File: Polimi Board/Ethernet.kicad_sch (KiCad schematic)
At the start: 20 parts, among them J6 RJ45_Wuerth_7499010121A, U3 LAN8742A, Y2 25MHz

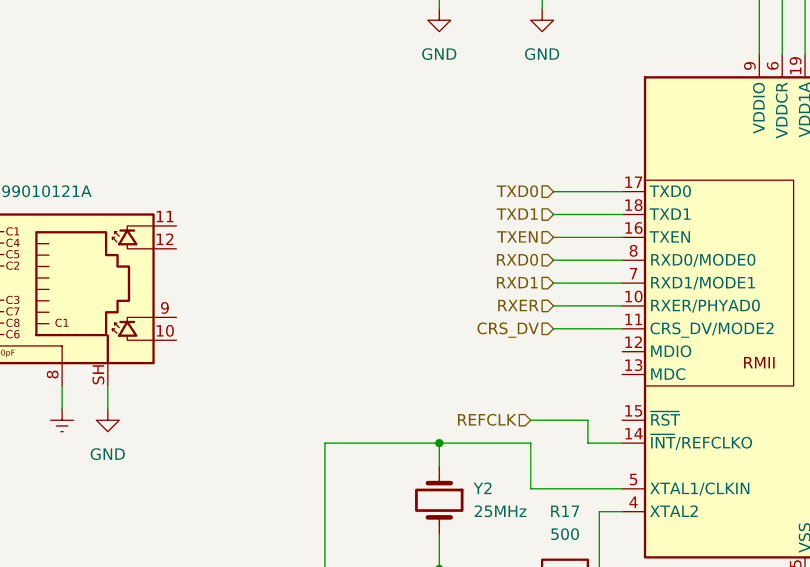
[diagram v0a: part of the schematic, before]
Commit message: Added GPIOs
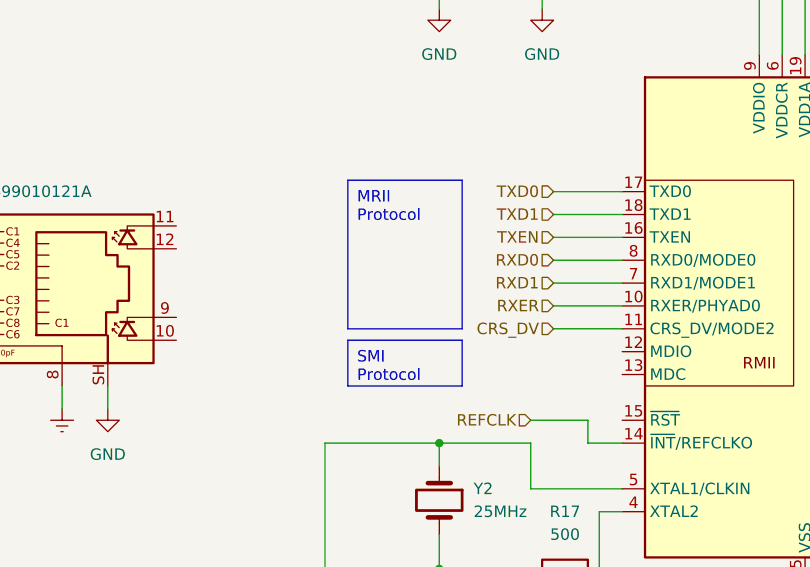
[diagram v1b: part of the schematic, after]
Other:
- company: (none) -> Politecnico di Milano
- title: (none) -> Polimi Board 
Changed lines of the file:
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@@
 (kicad_sch (version 20230121) (generator eeschema)
   (paper "A4")
+  (title_block
+    (title "Polimi Board ")
+    (date "2024-04-09")
+    (rev "1.0")
+    (company "Politecnico di Milano")
+    (comment 1 "Embedded Systems")
+    (comment 2 "ing. Zaccaria Eliseo Carrettoni")
+  )
   (junction (at 199.39 72.39) (diameter 0) (color 0 0 0 0)
   )
@@
     (stroke (width 0) (type default))
   )
+  (text_box "MRII\nProtocol\n"
+    (at 101.6 88.9 0) (size 12.7 16.51)
+    (stroke (width 0) (type default))
+    (fill (type none))
+    (effects (font (size 1.27 1.27)) (justify left top))
+  )
+  (text_box "SMI \nProtocol\n"
+    (at 101.6 106.68 0) (size 12.7 5.08)
+    (stroke (width 0) (type default))
+    (fill (type none))
+    (effects (font (size 1.27 1.27)) (justify left top))
+  )
   (label "TXN" (at 34.29 99.06 180) (fields_autoplaced)

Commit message: Finish schematic part
To be reviewd
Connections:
- no-connect marks 0 -> 8

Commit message: Fatte modifiche
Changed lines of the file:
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@@
   (title_block
     (title "Polimi Board ")
-    (date "2024-04-24")
-    (rev "1.0")
+    (date "2024-04-29")
+    (rev "2.0")
     (company "Politecnico di Milano")
     (comment 1 "Embedded Systems Project")
@@
     (stroke (width 0) (type default))
   )
-  (text_box "MRII\nProtocol\n"
+  (text_box "RMII\nProtocol\n"
     (at 101.6 88.9 0) (size 12.7 16.51)
     (stroke (width 0) (type default))

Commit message: Update the design with new specifications
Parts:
- removed C22, C23: 10pF, symbol Device:C
- removed R17: 500, symbol Device:R
- removed Y2: 25MHz, symbol Device:Crystal
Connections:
- net MCO: now reaches U3.5 (XTAL1/CLKIN)
- no-connect marks 8 -> 9
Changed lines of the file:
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@@
   (title_block
     (title "Polimi Board ")
-    (date "2024-04-29")
+    (date "2024-05-14")
     (rev "2.0")
     (company "Politecnico di Milano")
@@
   (junction (at 123.19 34.29) (diameter 0) (color 0 0 0 0)
   )
-  (junction (at 111.76 118.11) (diameter 0) (color 0 0 0 0)
-  )
   (junction (at 204.47 97.79) (diameter 0) (color 0 0 0 0)
   )
   (junction (at 165.1 59.69) (diameter 0) (color 0 0 0 0)
   )
-  (junction (at 111.76 140.97) (diameter 0) (color 0 0 0 0)
-  )
   (junction (at 26.67 96.52) (diameter 0) (color 0 0 0 0)
   )
@@
   )
   (junction (at 204.47 72.39) (diameter 0) (color 0 0 0 0)
-  )
-  (junction (at 111.76 132.08) (diameter 0) (color 0 0 0 0)
   )
   (junction (at 123.19 59.69) (diameter 0) (color 0 0 0 0)
@@
   (no_connect (at 132.08 107.95))
   (no_connect (at 132.08 115.57))
+  (no_connect (at 132.08 125.73))
   (no_connect (at 82.55 106.68))
   (no_connect (at 82.55 104.14))
@@
     (stroke (width 0) (type default))
   )
-  (wire (pts (xy 111.76 128.27) (xy 111.76 132.08))
-    (stroke (width 0) (type default))
-  )
-  (wire (pts (xy 121.92 123.19) (xy 121.92 118.11))
-    (stroke (width 0) (type default))
-  )
   (wire (pts (xy 165.1 67.31) (xy 165.1 69.85))
     (stroke (width 0) (type default))
@@
     (stroke (width 0) (type default))
   )
-  (wire (pts (xy 111.76 139.7) (xy 111.76 140.97))
-    (stroke (width 0) (type default))
-  )
   (wire (pts (xy 204.47 97.79) (xy 207.01 97.79))
     (stroke (width 0) (type default))
@@
     (stroke (width 0) (type default))
   )
-  (wire (pts (xy 128.27 118.11) (xy 132.08 118.11))
+  (wire (pts (xy 124.46 118.11) (xy 132.08 118.11))
     (stroke (width 0) (type default))
   )
@@
     (stroke (width 0) (type default))
   )
-  (wire (pts (xy 121.92 115.57) (xy 128.27 115.57))
-    (stroke (width 0) (type default))
-  )
-  (wire (pts (xy 132.08 125.73) (xy 129.54 125.73))
-    (stroke (width 0) (type default))
-  )
   (wire (pts (xy 34.29 101.6) (xy 39.37 101.6))
     (stroke (width 0) (type default))
   )
-  (wire (pts (xy 99.06 139.7) (xy 99.06 140.97))
+  (wire (pts (xy 124.46 123.19) (xy 132.08 123.19))
     (stroke (width 0) (type default))
   )
@@
     (stroke (width 0) (type default))
   )
-  (wire (pts (xy 111.76 118.11) (xy 111.76 120.65))
-    (stroke (width 0) (type default))
-  )
   (wire (pts (xy 74.93 111.76) (xy 74.93 124.46))
     (stroke (width 0) (type default))
@@
     (stroke (width 0) (type default))
   )
-  (wire (pts (xy 129.54 125.73) (xy 129.54 132.08))
-    (stroke (width 0) (type default))
-  )
   (wire (pts (xy 26.67 104.14) (xy 39.37 104.14))
     (stroke (width 0) (type default))
@@
     (stroke (width 0) (type default))
   )
-  (wire (pts (xy 128.27 115.57) (xy 128.27 118.11))
-    (stroke (width 0) (type default))
-  )
   (wire (pts (xy 123.19 67.31) (xy 123.19 69.85))
     (stroke (width 0) (type default))
@@
     (stroke (width 0) (type default))
   )
-  (wire (pts (xy 111.76 132.08) (xy 121.92 132.08))
-    (stroke (width 0) (type default))
-  )
   (wire (pts (xy 170.18 100.33) (xy 213.36 100.33))
     (stroke (width 0) (type default))
@@
     (stroke (width 0) (type default))
   )
-  (wire (pts (xy 111.76 118.11) (xy 99.06 118.11))
-    (stroke (width 0) (type default))
-  )
   (wire (pts (xy 124.46 90.17) (xy 132.08 90.17))
     (stroke (width 0) (type default))
   )
-  (wire (pts (xy 99.06 118.11) (xy 99.06 132.08))
-    (stroke (width 0) (type default))
-  )
-  (wire (pts (xy 132.08 123.19) (xy 121.92 123.19))
-    (stroke (width 0) (type default))
-  )
   (wire (pts (xy 194.31 82.55) (xy 194.31 95.25))
     (stroke (width 0) (type default))
   )
-  (wire (pts (xy 99.06 140.97) (xy 111.76 140.97))
-    (stroke (width 0) (type default))
-  )
   (wire (pts (xy 175.26 123.19) (xy 175.26 127))
     (stroke (width 0) (type default))
@@
   )
   (wire (pts (xy 170.18 95.25) (xy 194.31 95.25))
-    (stroke (width 0) (type default))
-  )
-  (wire (pts (xy 121.92 118.11) (xy 111.76 118.11))
-    (stroke (width 0) (type default))
-  )
-  (wire (pts (xy 111.76 140.97) (xy 111.76 142.24))
     (stroke (width 0) (type default))
   )
@@
     (effects (font (size 1.27 1.27)) (justify left top))
   )
+  (text_box "MCO\nClock from MCU\n"
+    (at 101.6 119.38 0) (size 12.7 7.62)
+    (stroke (width 0) (type default))
+    (fill (type none))
+    (effects (font (size 1.27 1.27)) (justify left top))
+  )
   (label "TXN" (at 34.29 99.06 180) (fields_autoplaced)
     (effects (font (size 1.27 1.27)) (justify right bottom))
@@
     (effects (font (size 1.27 1.27)) (justify right bottom))
   )
-  (hierarchical_label "REFCLK" (shape input) (at 121.92 115.57 180) (fields_autoplaced)
+  (hierarchical_label "REFCLK" (shape input) (at 124.46 118.11 180) (fields_autoplaced)
     (effects (font (size 1.27 1.27)) (justify right))
   )
@@
     (effects (font (size 1.27 1.27)) (justify right))
   )
+  (hierarchical_label "MCO" (shape input) (at 124.46 123.19 180) (fields_autoplaced)
+    (effects (font (size 1.27 1.27)) (justify right))
+  )
   (hierarchical_label "RXER" (shape input) (at 124.46 102.87 180) (fields_autoplaced)
     (effects (font (size 1.27 1.27)) (justify right))
@@
     )
   )
-  (symbol (lib_id "Device:R") (at 125.73 132.08 90) (unit 1)
-    (in_bom yes) (on_board yes) (dnp no) (fields_autoplaced)
-    (property "Reference" "R17" (at 125.73 125.73 90)
-      (effects (font (size 1.27 1.27)))
-    )
-    (property "Value" "500" (at 125.73 128.27 90)
-      (effects (font (size 1.27 1.27)))
-    )
-    (property "Footprint" "" (at 125.73 133.858 90)
-      (effects (font (size 1.27 1.27)) hide)
-    )
-    (property "Datasheet" "~" (at 125.73 132.08 0)
-      (effects (font (size 1.27 1.27)) hide)
-    )
-    (pin "2")
-    (pin "1")
-    (instances
-      (project "Polimi Board"
-        (path "/319fe76e-1f98-44b3-99b0-af1a9ad7322c/2985c2dc-97fe-4379-8500-18b000a93b2c"
-          (reference "R17") (unit 1)
-        )
-      )
-    )
-  )
   (symbol (lib_id "Device:R") (at 204.47 78.74 0) (unit 1)
     (in_bom yes) (on_board yes) (dnp no) (fields_autoplaced)
@@
         (path "/319fe76e-1f98-44b3-99b0-af1a9ad7322c/2985c2dc-97fe-4379-8500-18b000a93b2c"
           (reference "#PWR046") (unit 1)
-        )
-      )
-    )
-  )
-  (symbol (lib_id "power:GND") (at 111.76 142.24 0) (unit 1)
-    (in_bom yes) (on_board yes) (dnp no) (fields_autoplaced)
-    (property "Reference" "#PWR052" (at 111.76 148.59 0)
-      (effects (font (size 1.27 1.27)) hide)
-    )
-    (property "Value" "GND" (at 111.76 147.32 0)
-      (effects (font (size 1.27 1.27)))
-    )
-    (property "Footprint" "" (at 111.76 142.24 0)
-      (effects (font (size 1.27 1.27)) hide)
-    )
-    (property "Datasheet" "" (at 111.76 142.24 0)
-      (effects (font (size 1.27 1.27)) hide)
-    )
-    (pin "1")
-    (instances
-      (project "Polimi Board"
-        (path "/319fe76e-1f98-44b3-99b0-af1a9ad7322c/2985c2dc-97fe-4379-8500-18b000a93b2c"
-          (reference "#PWR052") (unit 1)
         )
       )
@@
     )
   )
-  (symbol (lib_id "Device:C") (at 99.06 135.89 0) (unit 1)
-    (in_bom yes) (on_board yes) (dnp no) (fields_autoplaced)
-    (property "Reference" "C23" (at 102.87 134.62 0)
-      (effects (font (size 1.27 1.27)) (justify left))
-    )
-    (property "Value" "10pF" (at 102.87 137.16 0)
-      (effects (font (size 1.27 1.27)) (justify left))
-    )
-    (property "Footprint" "" (at 100.0252 139.7 0)
-      (effects (font (size 1.27 1.27)) hide)
-    )
-    (property "Datasheet" "~" (at 99.06 135.89 0)
-      (effects (font (size 1.27 1.27)) hide)
-    )
-    (pin "1")
-    (pin "2")
-    (instances
-      (project "Polimi Board"
-        (path "/319fe76e-1f98-44b3-99b0-af1a9ad7322c/2985c2dc-97fe-4379-8500-18b000a93b2c"
-          (reference "C23") (unit 1)
-        )
-      )
-    )
-  )
   (symbol (lib_id "power:GND") (at 165.1 69.85 0) (unit 1)
     (in_bom yes) (on_board yes) (dnp no) (fields_autoplaced)
@@
     )
   )
-  (symbol (lib_id "Device:C") (at 111.76 135.89 0) (unit 1)
-    (in_bom yes) (on_board yes) (dnp no) (fields_autoplaced)
-    (property "Reference" "C22" (at 115.57 134.62 0)
-      (effects (font (size 1.27 1.27)) (justify left))
-    )
-    (property "Value" "10pF" (at 115.57 137.16 0)
-      (effects (font (size 1.27 1.27)) (justify left))
-    )
-    (property "Footprint" "" (at 112.7252 139.7 0)
-      (effects (font (size 1.27 1.27)) hide)
-    )
-    (property "Datasheet" "~" (at 111.76 135.89 0)
-      (effects (font (size 1.27 1.27)) hide)
-    )
-    (pin "1")
-    (pin "2")
-    (instances
-      (project "Polimi Board"
-        (path "/319fe76e-1f98-44b3-99b0-af1a9ad7322c/2985c2dc-97fe-4379-8500-18b000a93b2c"
-          (reference "C22") (unit 1)
-        )
-      )
-    )
-  )
   (symbol (lib_id "Device:C") (at 111.76 38.1 0) (unit 1)
     (in_bom yes) (on_board yes) (dnp no) (fields_autoplaced)
@@
         )
       )
-    )
-  )
-  (symbol (lib_id "Device:Crystal") (at 111.76 124.46 270) (unit 1)
-    (in_bom yes) (on_board yes) (dnp no) (fields_autoplaced)
-    (property "Reference" "Y2" (at 115.57 123.19 90)
-      (effects (font (size 1.27 1.27)) (justify left))
-    )
-    (property "Value" "25MHz" (at 115.57 125.73 90)
-      (effects (font (size 1.27 1.27)) (justify left))
-    )
-    (property "Footprint" "" (at 111.76 124.46 0)
-      (effects (font (size 1.27 1.27)) hide)
-    )
-    (property "Datasheet" "~" (at 111.76 124.46 0)
-      (effects (font (size 1.27 1.27)) hide)
-    )
-    (pin "2")
-    (pin "1")
-    (instances
-      (project "Polimi Board"
-        (path "/319fe76e-1f98-44b3-99b0-af1a9ad7322c/2985c2dc-97fe-4379-8500-18b000a93b2c"
-          (reference "Y2") (unit 1)
-        )
-      )

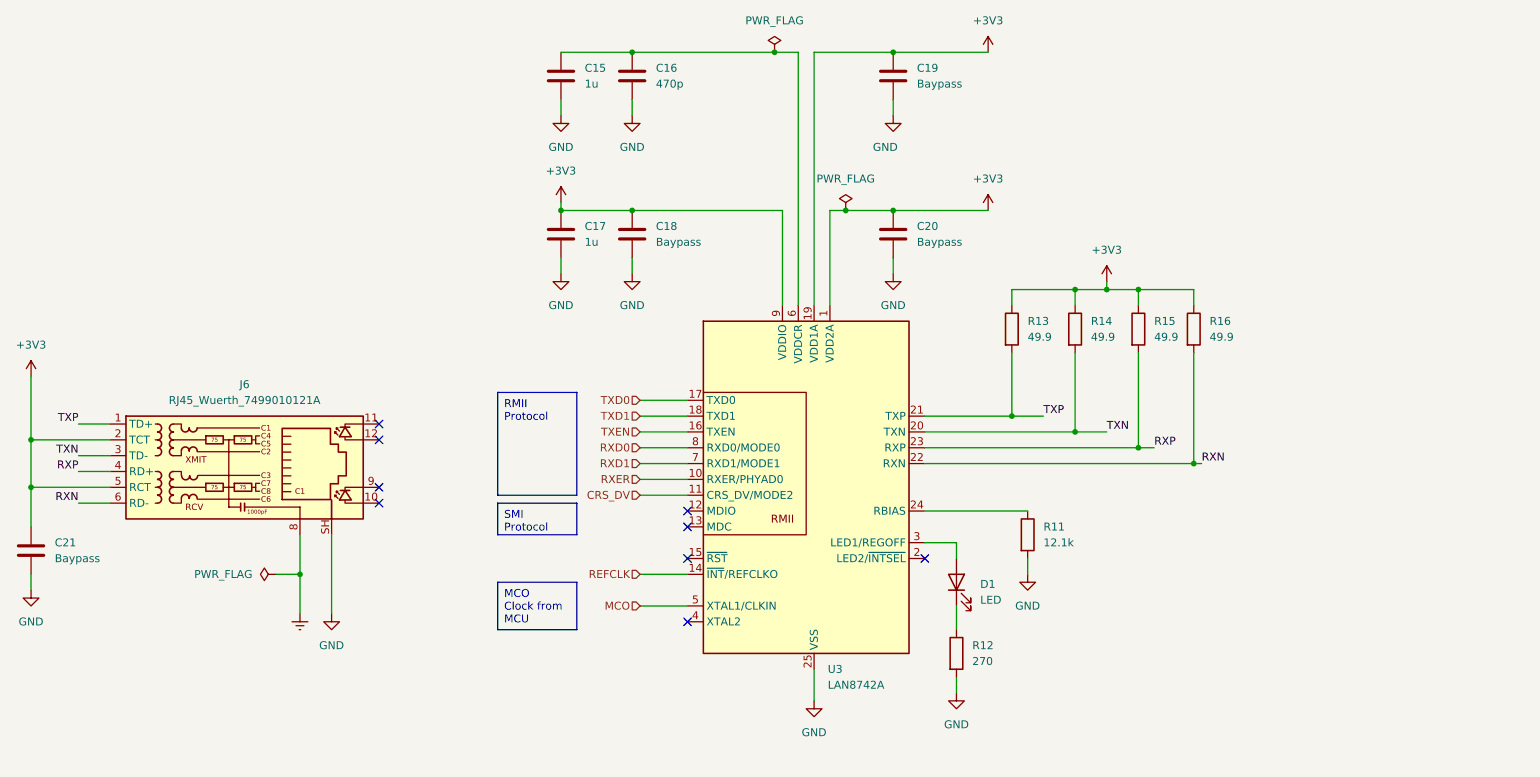
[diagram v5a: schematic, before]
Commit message: Adjusted Leds
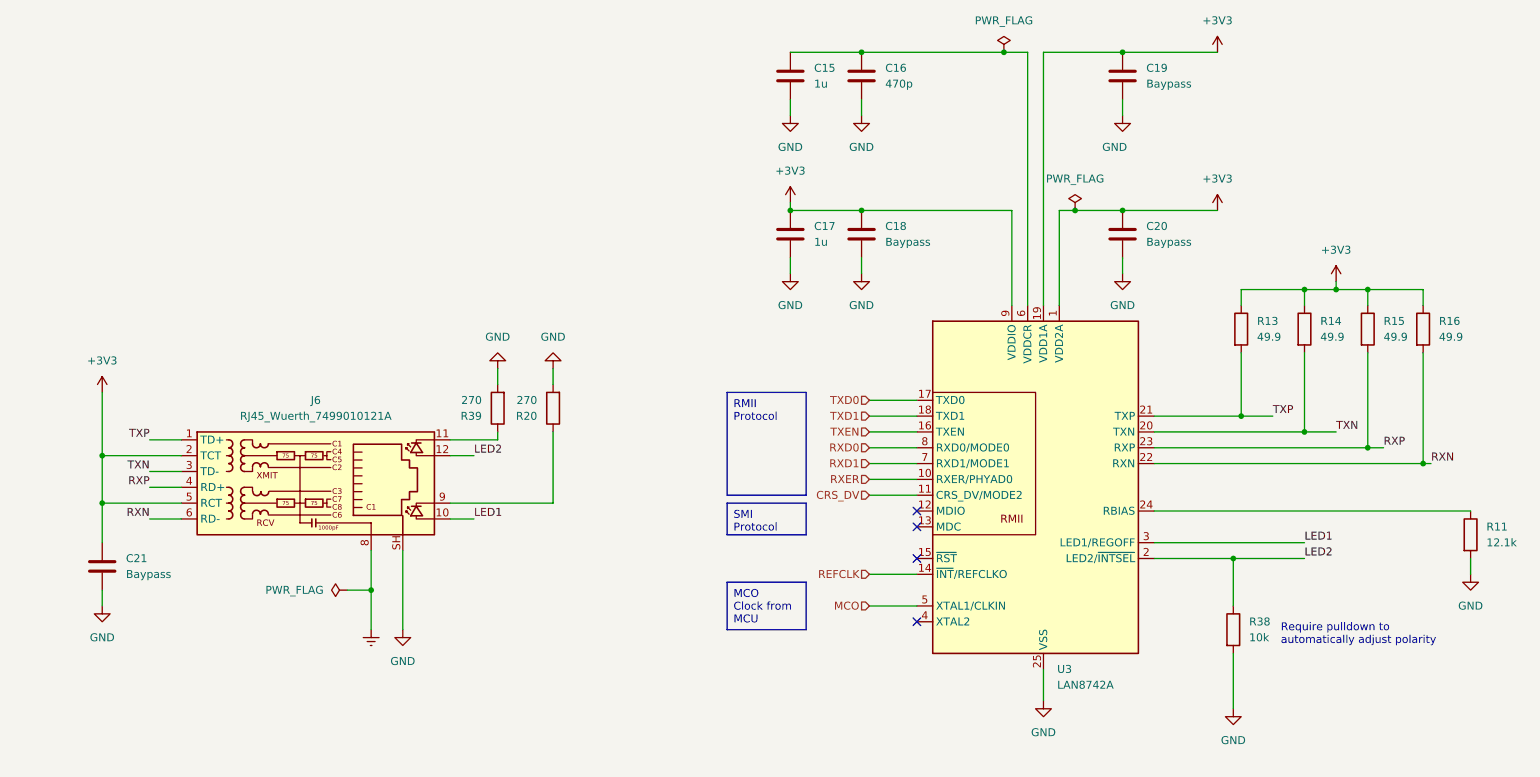
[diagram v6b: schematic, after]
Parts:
- removed D1: LED, symbol Device:LED
- removed R12: 270, symbol Device:R
- added R20, R39: 270, symbol Device:R
- added R38: 10k, symbol Device:R
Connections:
- net GND: now also R20.2, R38.2, R39.2
- net LED1: now reaches U3.3 (LED1/REGOFF)
- net LED1: now also J6.10
- net LED2: now reaches U3.2 (LED2/~{INTSEL})
- net LED2: now also J6.12, R38.1
- net at J6.11: now also R39.1
- net at J6.9: now also R20.1
- no-connect marks 9 -> 4
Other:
- note added: "Require pulldown to automatically adjust polarity"
- moved on the sheet: C15, C16, C17, C18, C19, C20, C21, J6, R11, R13, R14, R15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

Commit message: Added changes to the design
Ready for pcb design
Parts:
- C15, C17: value 1u -> 1uF
- C16: value 470p -> 470pF
- C18, C19, C20, C21: value Baypass -> 100nF
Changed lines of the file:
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@@
   (title_block
     (title "Polimi Board ")
-    (date "2024-05-15")
+    (date "2024-07-16")
     (rev "2.0")
     (company "Politecnico di Milano")
@@
       (effects (font (size 1.27 1.27)) (justify left))
     )
-    (property "Value" "470p" (at 163.83 39.37 0)
+    (property "Value" "470pF" (at 163.83 39.37 0)
       (effects (font (size 1.27 1.27)) (justify left))
     )
@@
       (effects (font (size 1.27 1.27)) (justify left))
     )
-    (property "Value" "Baypass" (at 163.83 64.77 0)
+    (property "Value" "100nF" (at 163.83 64.77 0)
       (effects (font (size 1.27 1.27)) (justify left))
     )
@@
       (effects (font (size 1.27 1.27)) (justify left))
     )
-    (property "Value" "Baypass" (at 205.74 39.37 0)
+    (property "Value" "100nF" (at 205.74 39.37 0)
       (effects (font (size 1.27 1.27)) (justify left))
     )
@@
       (effects (font (size 1.27 1.27)) (justify left))
     )
-    (property "Value" "Baypass" (at 41.91 118.11 0)
+    (property "Value" "100nF" (at 41.91 118.11 0)
       (effects (font (size 1.27 1.27)) (justify left))
     )
@@
       (effects (font (size 1.27 1.27)) (justify left))
     )
-    (property "Value" "Baypass" (at 205.74 64.77 0)
+    (property "Value" "100nF" (at 205.74 64.77 0)
       (effects (font (size 1.27 1.27)) (justify left))
     )
@@
       (effects (font (size 1.27 1.27)) (justify left))
     )
-    (property "Value" "1u" (at 152.4 39.37 0)
+    (property "Value" "1uF" (at 152.4 39.37 0)
       (effects (font (size 1.27 1.27)) (justify left))
     )
@@
       (effects (font (size 1.27 1.27)) (justify left))
     )
-    (property "Value" "1u" (at 152.4 64.77 0)
-      (effects (font (size 1.27 1.27)) (justify left))
-    )
+    (property "Value" "1uF" (at 152.4 64.77 0)
+      (effects (font (size 1.27 1.27)) (justify left))
+    )
